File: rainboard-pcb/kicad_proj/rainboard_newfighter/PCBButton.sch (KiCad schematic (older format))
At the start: 4 parts, among them SW1 SANWA-OBSF24

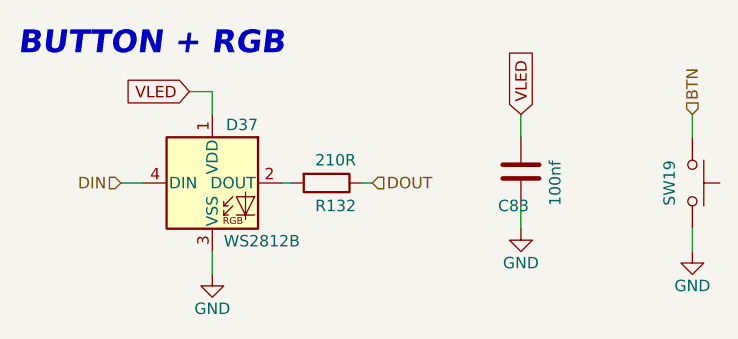
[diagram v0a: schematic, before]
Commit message: Moves meta button connectors to correct spots
Updates locations for layout to continue
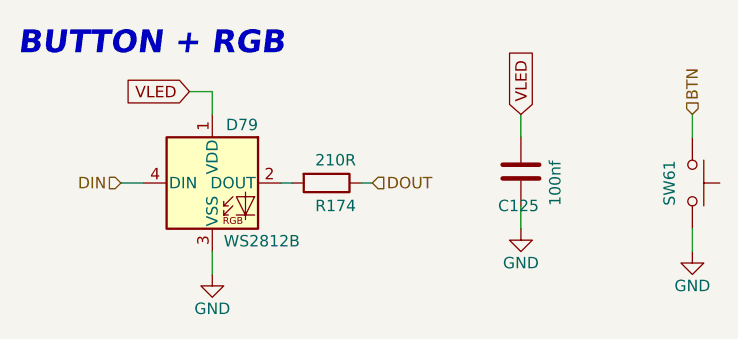
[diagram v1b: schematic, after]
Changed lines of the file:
@@
 AR Path="/6016C70A/611F5597/5FE1B43A" Ref="SW60"  Part="1"
 AR Path="/6016C70A/6120995F/5FE1B43A" Ref="SW61"  Part="1"
-F 0 "SW19" H 3600 1300 50  0000 C CNN
+F 0 "SW61" H 3600 1300 50  0000 C CNN
 F 1 "SANWA-OBSF24" H 3600 1340 50  0001 C CNN
 F 2 "rainboard_fp:Sanwa-OBSF24-v2" H 3600 1600 50  0001 C CNN
@@
 AR Path="/6016C70A/611F5597/5FE1B440" Ref="D78"  Part="1"
 AR Path="/6016C70A/6120995F/5FE1B440" Ref="D79"  Part="1"
-F 0 "D37" H 1700 1625 50  0000 R BNN
+F 0 "D79" H 1700 1625 50  0000 R BNN
 F 1 "WS2812B" H 1550 1175 50  0000 L TNN
 F 2 "LED_SMD:LED_WS2812B_PLCC4_5.0x5.0mm_P3.2mm" H 1550 1100 50  0001 L TNN
@@
 AR Path="/6016C70A/611F5597/5FE1B446" Ref="#PWR0291"  Part="1"
 AR Path="/6016C70A/6120995F/5FE1B446" Ref="#PWR0294"  Part="1"
-F 0 "#PWR0168" H 3600 1450 50  0001 C CNN
+F 0 "#PWR0294" H 3600 1450 50  0001 C CNN
 F 1 "GND" H 3600 1550 50  0000 C CNN
 F 2 "" H 3600 1700 50  0001 C CNN
@@
 AR Path="/6016C70A/611F5597/5FE1B44C" Ref="#PWR0289"  Part="1"
 AR Path="/6016C70A/6120995F/5FE1B44C" Ref="#PWR0292"  Part="1"
-F 0 "#PWR0166" H 1500 1550 50  0001 C CNN
+F 0 "#PWR0292" H 1500 1550 50  0001 C CNN
 F 1 "GND" H 1500 1650 50  0000 C CNN
 F 2 "" H 1500 1800 50  0001 C CNN
@@
 AR Path="/6016C70A/611F5597/5FE1B462" Ref="R173"  Part="1"
 AR Path="/6016C70A/6120995F/5FE1B462" Ref="R174"  Part="1"
-F 0 "R132" V 2100 1350 50  0000 L CNN
+F 0 "R174" V 2100 1350 50  0000 L CNN
 F 1 "210R" V 1900 1350 50  0000 L CNN
 F 2 "Resistor_SMD:R_0805_2012Metric" V 1930 1400 50  0001 C CNN
@@
 AR Path="/6016C70A/611F5597/5FE25316" Ref="C124"  Part="1"
 AR Path="/6016C70A/6120995F/5FE25316" Ref="C125"  Part="1"
-F 0 "C83" H 2750 1200 50  0000 L CNN
+F 0 "C125" H 2750 1200 50  0000 L CNN
 F 1 "100nf" V 3000 1200 50  0000 L CNN
 F 2 "Capacitor_SMD:C_0603_1608Metric" H 2888 1200 50  0001 C CNN
@@
 AR Path="/6016C70A/611F5597/5FE292FC" Ref="#PWR0290"  Part="1"
 AR Path="/6016C70A/6120995F/5FE292FC" Ref="#PWR0293"  Part="1"
-F 0 "#PWR0167" H 2850 1350 50  0001 C CNN
+F 0 "#PWR0293" H 2850 1350 50  0001 C CNN
 F 1 "GND" H 2850 1450 50  0000 C CNN
 F 2 "" H 2850 1600 50  0001 C CNN

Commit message: Review and gerber export of v1a
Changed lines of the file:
@@
 $Descr A4 11693 8268
 encoding utf-8
-Sheet 21 63
+Sheet 49 63
 Title ""
 Date ""
@@
 AR Path="/6016C70A/611F5597/5FE1B43A" Ref="SW60"  Part="1"
 AR Path="/6016C70A/6120995F/5FE1B43A" Ref="SW61"  Part="1"
-F 0 "SW61" H 3600 1300 50  0000 C CNN
+F 0 "SW47" H 3600 1300 50  0000 C CNN
 F 1 "SANWA-OBSF24" H 3600 1340 50  0001 C CNN
 F 2 "rainboard_fp:Sanwa-OBSF24-v2" H 3600 1600 50  0001 C CNN
@@
 AR Path="/6016C70A/611F5597/5FE1B440" Ref="D78"  Part="1"
 AR Path="/6016C70A/6120995F/5FE1B440" Ref="D79"  Part="1"
-F 0 "D79" H 1700 1625 50  0000 R BNN
+F 0 "D65" H 1700 1625 50  0000 R BNN
 F 1 "WS2812B" H 1550 1175 50  0000 L TNN
 F 2 "LED_SMD:LED_WS2812B_PLCC4_5.0x5.0mm_P3.2mm" H 1550 1100 50  0001 L TNN
@@
 AR Path="/6016C70A/611F5597/5FE1B446" Ref="#PWR0291"  Part="1"
 AR Path="/6016C70A/6120995F/5FE1B446" Ref="#PWR0294"  Part="1"
-F 0 "#PWR0294" H 3600 1450 50  0001 C CNN
+F 0 "#PWR0252" H 3600 1450 50  0001 C CNN
 F 1 "GND" H 3600 1550 50  0000 C CNN
 F 2 "" H 3600 1700 50  0001 C CNN
@@
 AR Path="/6016C70A/611F5597/5FE1B44C" Ref="#PWR0289"  Part="1"
 AR Path="/6016C70A/6120995F/5FE1B44C" Ref="#PWR0292"  Part="1"
-F 0 "#PWR0292" H 1500 1550 50  0001 C CNN
+F 0 "#PWR0250" H 1500 1550 50  0001 C CNN
 F 1 "GND" H 1500 1650 50  0000 C CNN
 F 2 "" H 1500 1800 50  0001 C CNN
@@
 AR Path="/6016C70A/611F5597/5FE1B462" Ref="R173"  Part="1"
 AR Path="/6016C70A/6120995F/5FE1B462" Ref="R174"  Part="1"
-F 0 "R174" V 2100 1350 50  0000 L CNN
+F 0 "R160" V 2100 1350 50  0000 L CNN
 F 1 "210R" V 1900 1350 50  0000 L CNN
 F 2 "Resistor_SMD:R_0805_2012Metric" V 1930 1400 50  0001 C CNN
@@
 AR Path="/6016C70A/611F5597/5FE25316" Ref="C124"  Part="1"
 AR Path="/6016C70A/6120995F/5FE25316" Ref="C125"  Part="1"
-F 0 "C125" H 2750 1200 50  0000 L CNN
+F 0 "C111" H 2750 1200 50  0000 L CNN
 F 1 "100nf" V 3000 1200 50  0000 L CNN
 F 2 "Capacitor_SMD:C_0603_1608Metric" H 2888 1200 50  0001 C CNN
@@
 AR Path="/6016C70A/611F5597/5FE292FC" Ref="#PWR0290"  Part="1"
 AR Path="/6016C70A/6120995F/5FE292FC" Ref="#PWR0293"  Part="1"
-F 0 "#PWR0293" H 2850 1350 50  0001 C CNN
+F 0 "#PWR0251" H 2850 1350 50  0001 C CNN
 F 1 "GND" H 2850 1450 50  0000 C CNN
 F 2 "" H 2850 1600 50  0001 C CNN
